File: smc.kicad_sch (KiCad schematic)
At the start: 29 parts

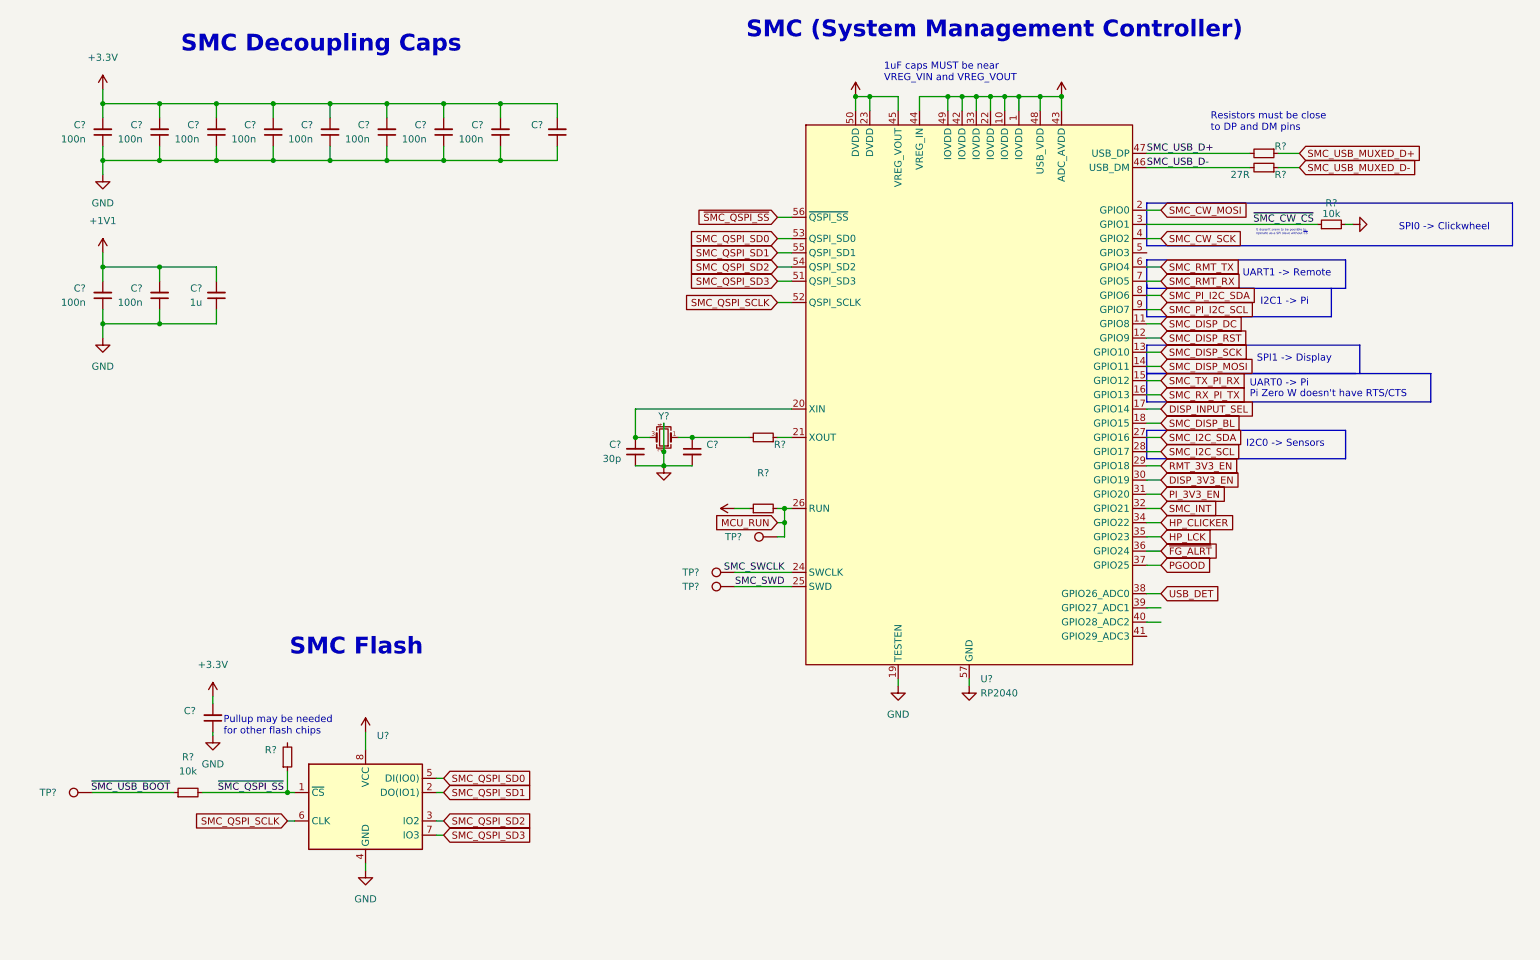
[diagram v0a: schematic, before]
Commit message: schem: first pass done, ERC passing
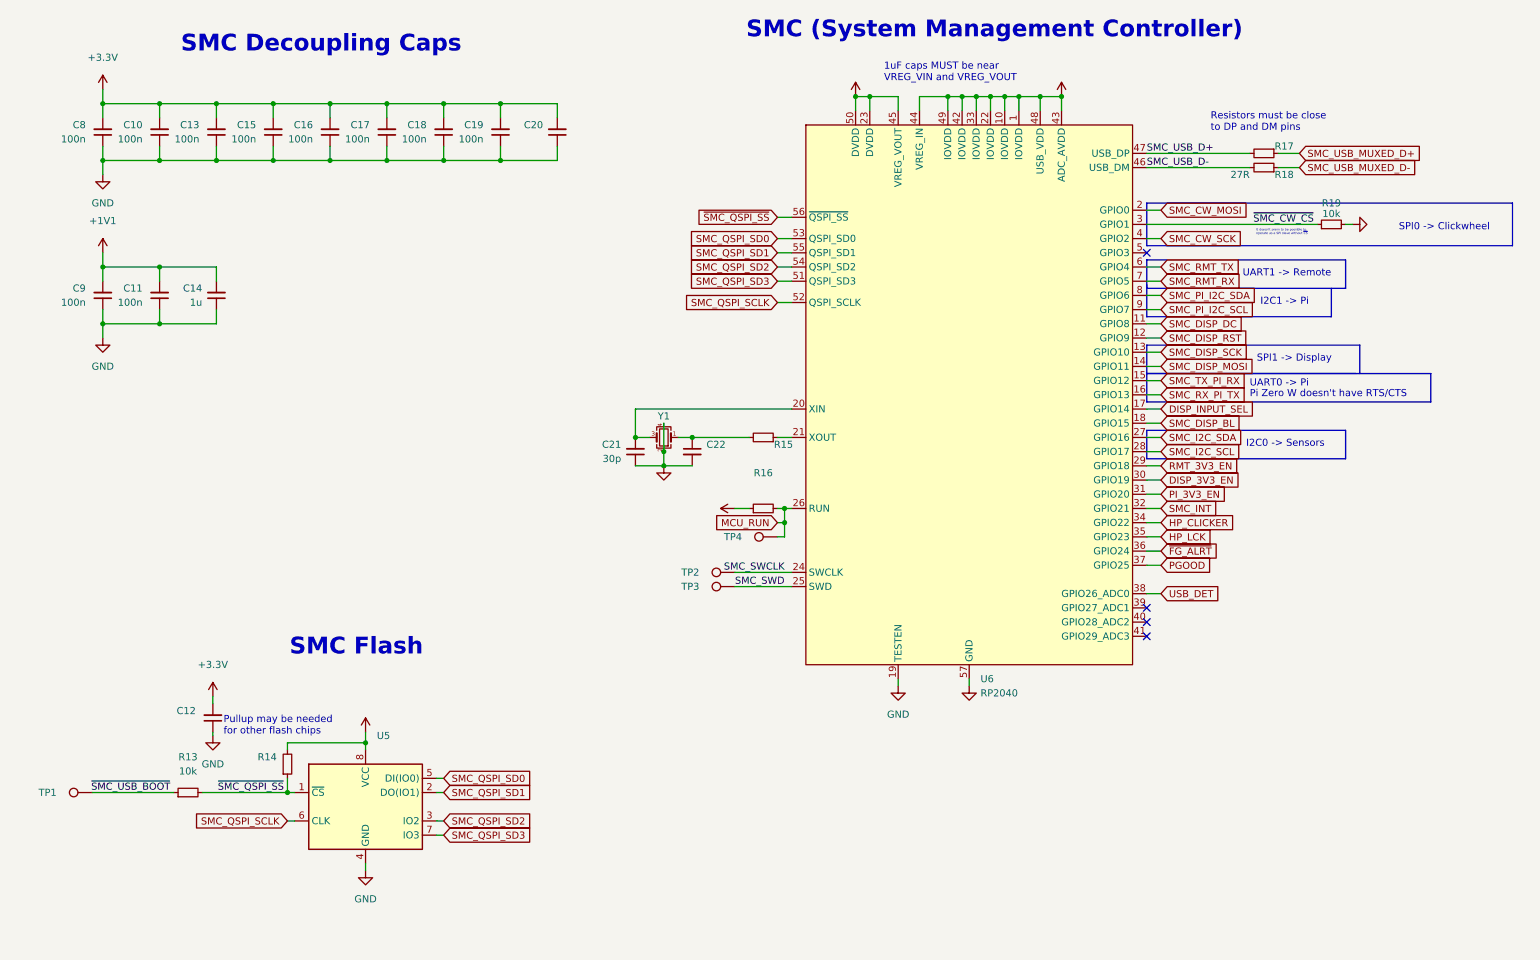
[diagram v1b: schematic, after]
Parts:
- U5: renamed from U?; footprint (none) -> Package_SO:SOIC-8_5.23x5.23mm_P1.27mm
- gave numbers to parts that had none: 28
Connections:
- net +3V3: now also R14.2
- no-connect marks 0 -> 4
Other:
- moved on the sheet: R14

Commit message: analysis: specify pi will be powered directly from VCC
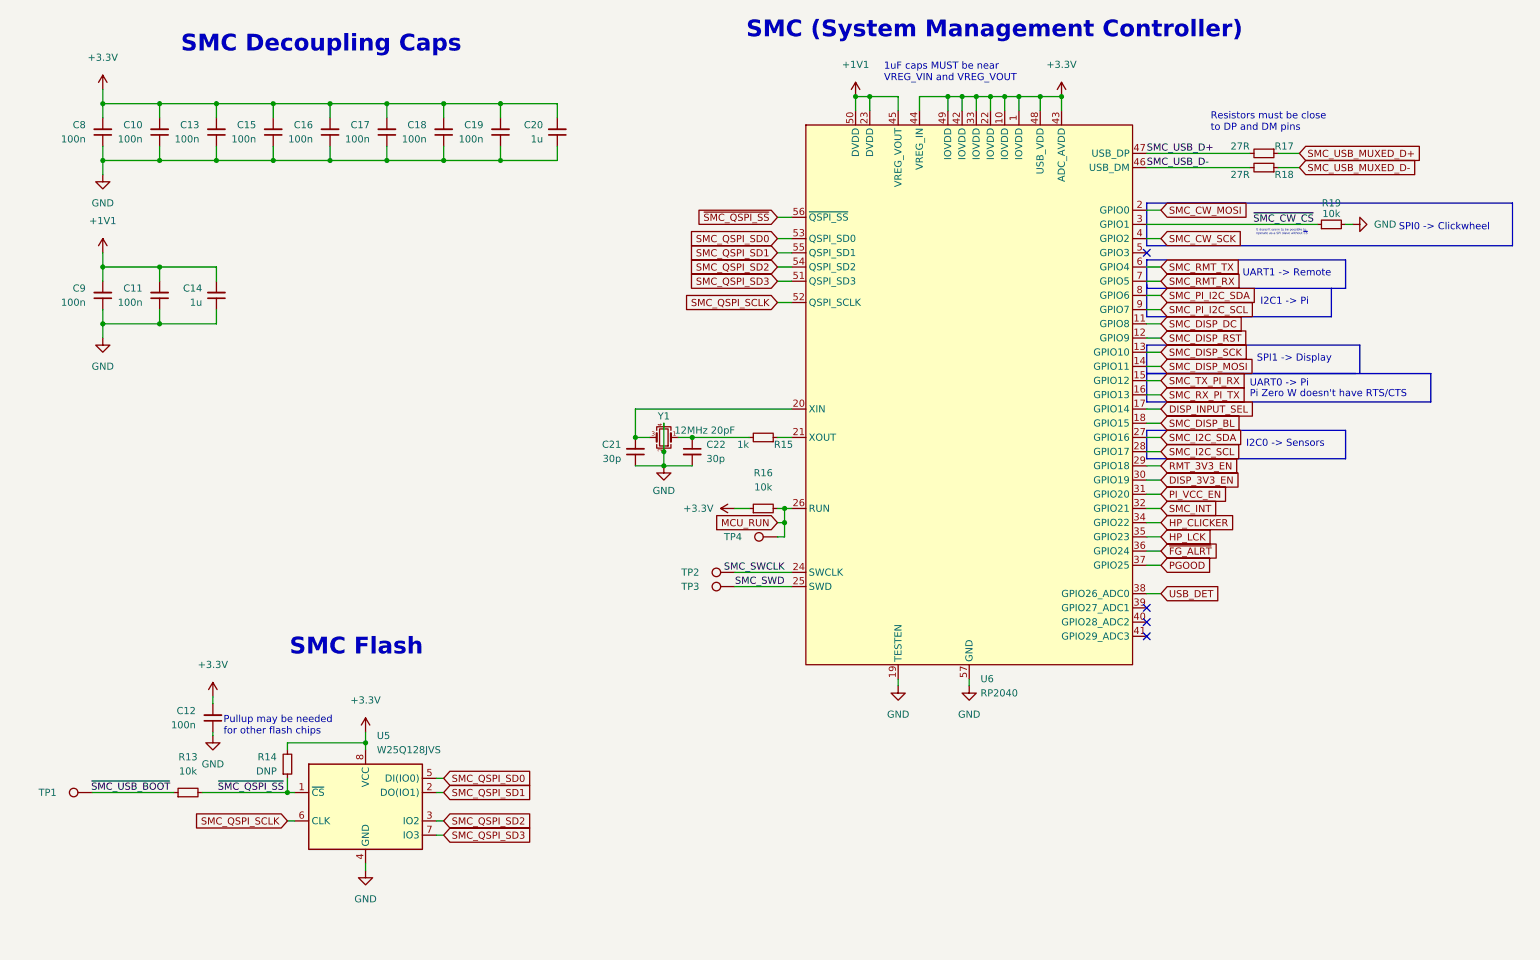
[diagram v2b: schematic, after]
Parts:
- C10, C11, C13, C14, C15, C16, C17, C18, C19, C21, C8, C9: footprint (none) -> Capacitor_SMD:C_0402_1005Metric
- C12: value (none) -> 100n; footprint (none) -> Capacitor_SMD:C_0402_1005Metric
- C20: value (none) -> 1u; footprint (none) -> Capacitor_SMD:C_0402_1005Metric
- C22: value (none) -> 30p; footprint (none) -> Capacitor_SMD:C_0402_1005Metric
- R13, R18, R19: footprint (none) -> Resistor_SMD:R_0402_1005Metric
- R14: value (none) -> DNP; footprint (none) -> Resistor_SMD:R_0402_1005Metric
- R15: value (none) -> 1k; footprint (none) -> Resistor_SMD:R_0402_1005Metric
- R16: value (none) -> 10k; footprint (none) -> Resistor_SMD:R_0402_1005Metric
- R17: value (none) -> 27R; footprint (none) -> Resistor_SMD:R_0402_1005Metric
- TP1, TP2, TP3, TP4: footprint (none) -> TestPoint:TestPoint_Pad_D1.5mm
- U5: value (none) -> W25Q128JVS
- Y1: value (none) -> 12MHz 20pF; footprint (none) -> Crystal:Crystal_SMD_5032-2Pin_5.0x3.2mm
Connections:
- net PI_3V3_EN renamed PI_VCC_EN

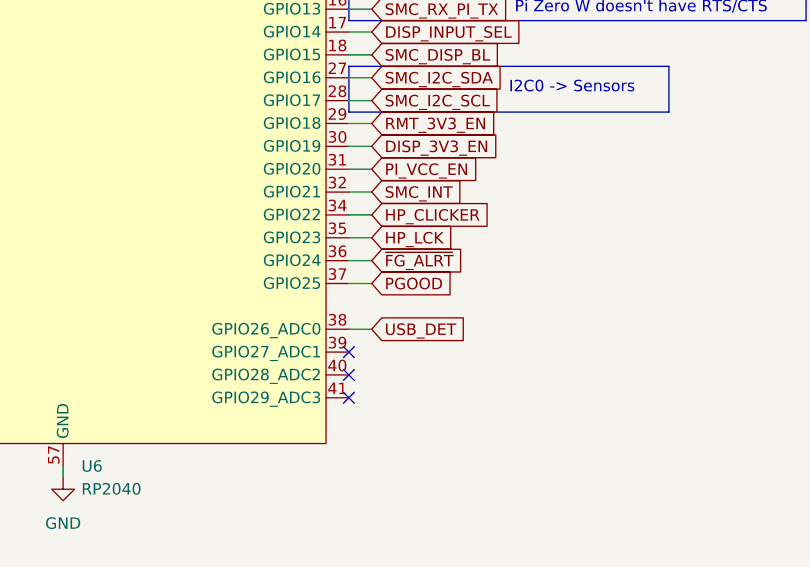
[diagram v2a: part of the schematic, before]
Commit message: analysis: change system regulator to one with lower dropout
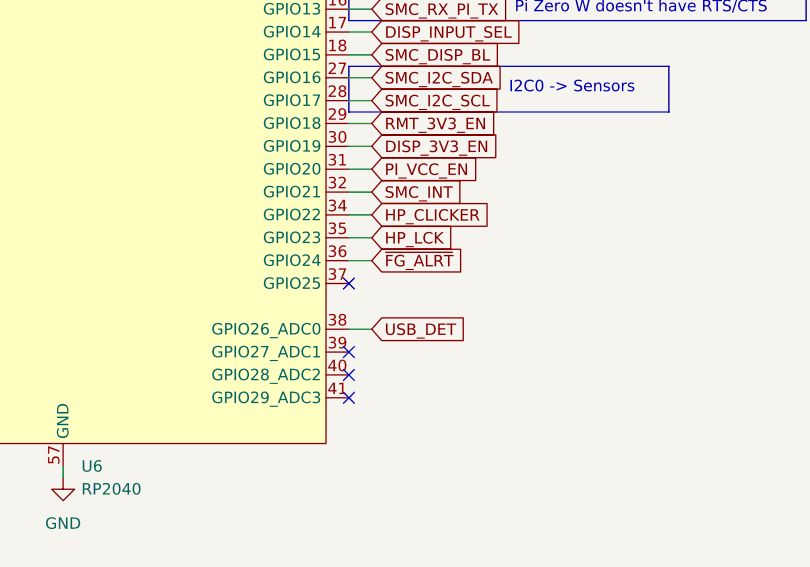
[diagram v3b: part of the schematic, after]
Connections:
- net PGOOD: no longer names the net of U6.37 (GPIO25)
- no-connect marks 4 -> 5
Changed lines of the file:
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@@
   (junction (at 30.48 54.61) (diameter 0) (color 0 0 0 0)
   )
+  (no_connect (at 217.17 127))
   (no_connect (at 217.17 71.12))
   (no_connect (at 217.17 139.7))
@@
     (stroke (width 0) (type default) (color 0 0 0 0))
   )
-  (wire (pts (xy 217.17 127) (xy 219.71 127))
-    (stroke (width 0) (type default) (color 0 0 0 0))
-  )
   (polyline (pts (xy 252.73 72.39) (xy 217.17 72.39))
     (stroke (width 0) (type default) (color 0 0 0 0))
@@
       (effects (font (size 1.27 1.27)) (justify left) hide)
     )
-  )
-  (global_label "PGOOD" (shape input) (at 219.71 127 0) (fields_autoplaced)
-    (effects (font (size 1.27 1.27)) (justify left))
-    (property "Intersheet References" "${INTERSHEET_REFS}" (id 0) (at 228.5941 127.0794 0)
-      (effects (font (size 1.27 1.27)) (justify left) hide)
-    )

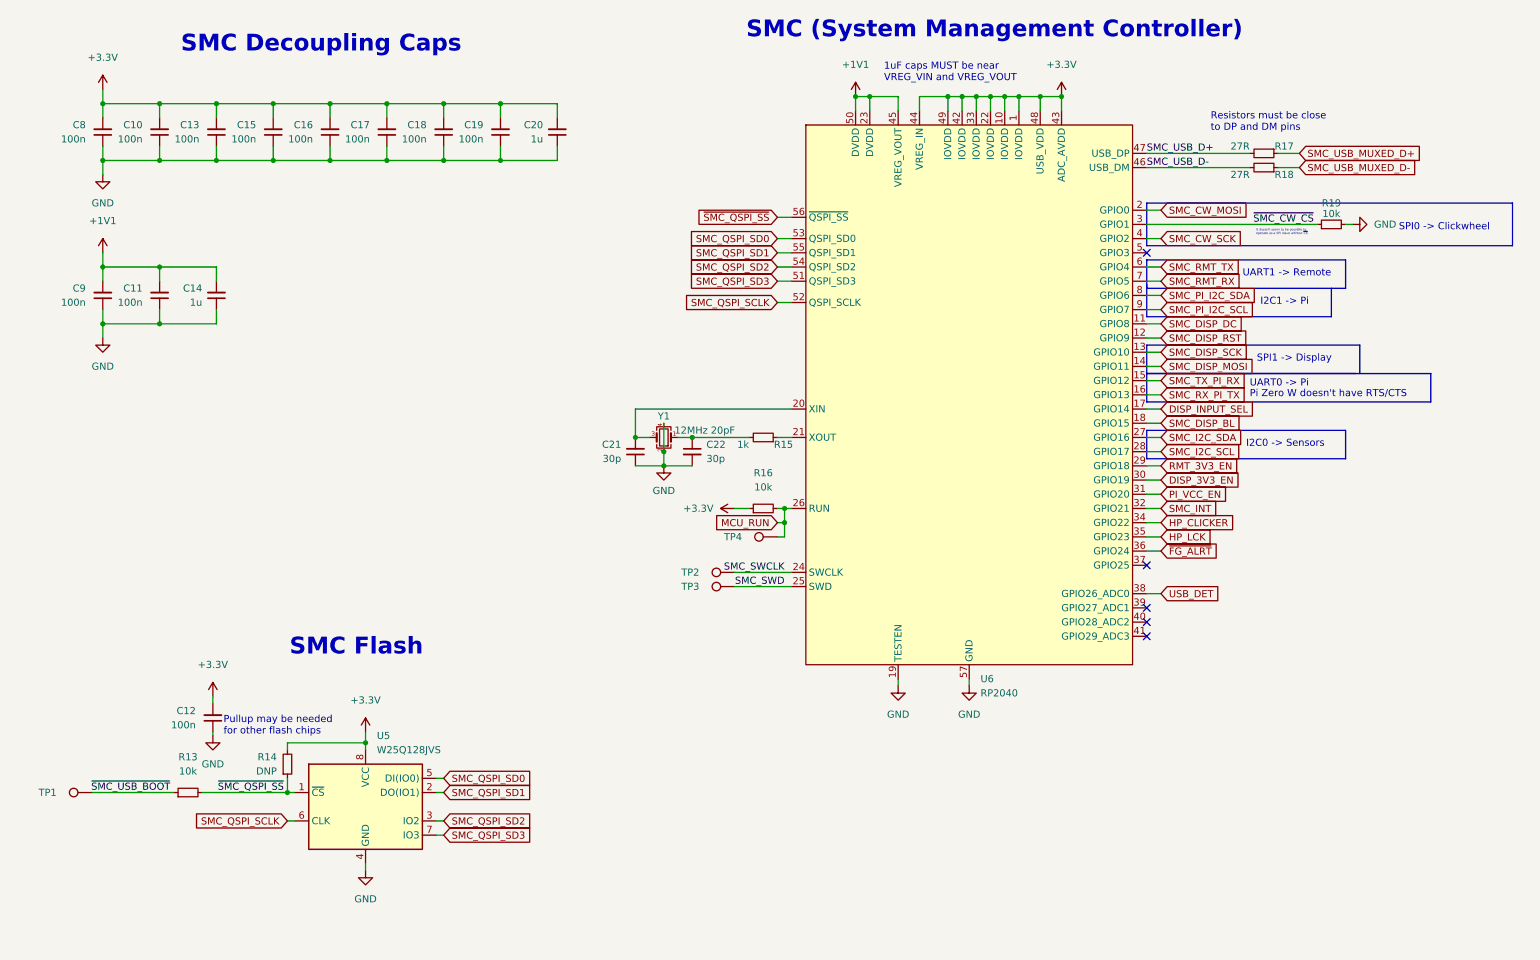
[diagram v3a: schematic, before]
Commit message: schem: migrate away from LCSC exclusive parts
- layout: migrate away from lcsc footprints
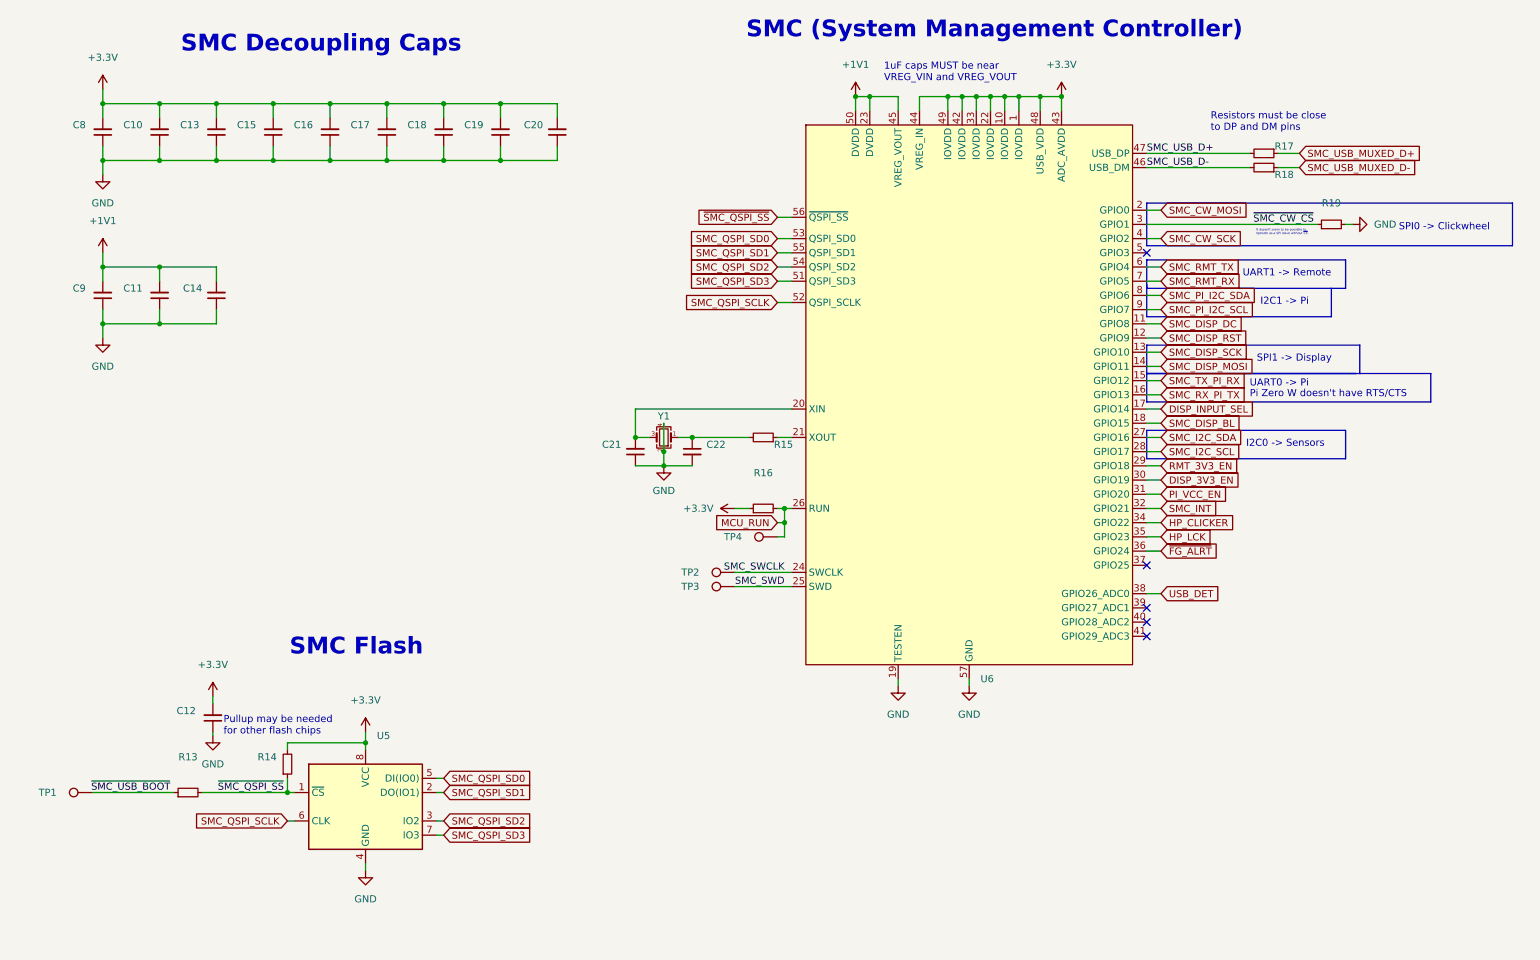
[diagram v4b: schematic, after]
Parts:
- C10, C11, C12, C13, C15, C16, C17, C18, C19, C8, C9: value 100n -> (none); footprint Capacitor_SMD:C_0402_1005Metric -> (none)
- C14, C20: value 1u -> (none); footprint Capacitor_SMD:C_0402_1005Metric -> (none)
- C21, C22: value 30p -> (none); footprint Capacitor_SMD:C_0402_1005Metric -> (none)
- R13, R16, R19: value 10k -> (none); footprint Resistor_SMD:R_0402_1005Metric -> (none)
- R14: value DNP -> (none); footprint Resistor_SMD:R_0402_1005Metric -> (none)
- R15: value 1k -> (none); footprint Resistor_SMD:R_0402_1005Metric -> (none)
- R17, R18: value 27R -> (none); footprint Resistor_SMD:R_0402_1005Metric -> (none)
- TP1, TP2, TP3, TP4: value TestPoint -> (none); footprint TestPoint:TestPoint_Pad_D1.5mm -> (none)
- U5: value W25Q128JVS -> (none); footprint Package_SO:SOIC-8_5.23x5.23mm_P1.27mm -> (none); Digikey Part (none) -> W25Q128JVSIMTR-ND; Digikey Price/Stock (none) -> https://www.digikey.ca/en/products/detail/winbond-electroni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; JLC Part (none) -> Extended Part; LCSC Part (none) -> C113767; Manufacturer (none) -> Winbond Electronics; Manufacturer Part (none) -> W25Q128JVS; Mouser Part (none) -> 454-W25Q128JVSIMTR; Mouser Price/Stock (none) -> https://www.mouser.ca/ProductDetail/Winbond/W25Q128JVSIM-TR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
- U6: value RP2040 -> (none); footprint lcsc:LQFN-56_L7.0-W7.0-P0.4-EP -> (none); Digikey Part (none) -> 2648-SC0914(13)TR-ND; Digikey Price/Stock (none) -> https://www.digikey.ca/en/products/detail/raspberry-pi/SC09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; Manufacturer Raspberry Pi(树莓派) -> Raspberry Pi; Manufacturer Part (none) -> RP2040; Mouser Part (none) -> RPI Chip RP2040-7-500; Mouser Price/Stock (none) -> https://www.mouser.ca/ProductDetail/Raspberry-Pi/RPI-Chip-R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
- Y1: value 12MHz 20pF -> (none); footprint Crystal:Crystal_SMD_5032-2Pin_5.0x3.2mm -> (none)
